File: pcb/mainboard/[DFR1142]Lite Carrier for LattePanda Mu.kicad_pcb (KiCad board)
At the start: 4 copper layers, 150 x 109 mm, 165 parts, among them J1 Conn_01x03_Pin, J10 Conn_01x03_Pin, J11 Conn_01x03_Pin, J12 Conn_01x04_Pin, J13 Conn_01x04_Pin, J14 Conn_01x03_Pin, J15 Bus_M.2_Socket_M, J16 Bus_M.2_Socket_E, J3 HDMI_A, J7 Conn_01x04_Pin, J78 Conn_01x02_Pin, J79 USB3_A, J8 Conn_01x03_Pin, J80 USB3_A, J81 USB_C_Receptacle_USB2.0_16P, J82 Conn_01x04_Pin, J83 Conn_01x02_Pin, J9 Conn_01x04_Pin, Q1 2N7002, Q2 2SK3018, Q3 2SK3018, Q4 2SK3018, Q8 2N7002, U1 TPAZ1023-04F, U10 ULC0524P, U11 ULC0524P, U12 ULC0524P, U15 SY8253ADC, U16 SY8253ADC, U2 TPAZ1023-04F, U3 ULC0524P, U4 ULC0524P, U5 ULC0524P, U78 ULC0524P, U9 ULC0524P

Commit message: a lot has been routed
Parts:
- moved C55 163.5 mm to (97.8, 137.0), turned to 90 degrees
- moved C56 161.3 mm to (96.8, 137.0), turned to 90 degrees
- moved J79 70.7 mm to (139.5, 155.3)
- moved J16 1.10 mm to (93.9, 118.0)
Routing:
- net /LattePanda Module/HSIO_3_TX-: track 0.00 -> 47.6 mm
- net /LattePanda Module/HSIO_3_TX+: track 0.00 -> 45.9 mm
- net /USB2.0&USB3.0/CON_USB4_SSRX_P: track 0.00 -> 40.2 mm, vias 0 -> 1
- net /USB2.0&USB3.0/CON_USB4_SSRX_N: track 0.00 -> 39.9 mm, vias 0 -> 1
- net /USB2.0&USB3.0/CON_USB3_SSRX_P: track 0.00 -> 35.4 mm, vias 0 -> 1
- net /USB2.0&USB3.0/CON_USB3_SSRX_N: track 0.00 -> 35.1 mm, vias 0 -> 1
- net /M.2 E&M Key/CON_PCIE_TX_0+: track 0.00 -> 11.6 mm, vias 0 -> 2
- net /M.2 E&M Key/CON_PCIE_TX_0-: track 0.00 -> 11.1 mm, vias 0 -> 2
- net /LattePanda Module/HSIO_3_RX-: track 43.1 -> 46.0 mm
- net /LattePanda Module/HSIO_3_RX+: track 42.5 -> 45.4 mm
- net /LattePanda Module/HSIO_2_RX+: track 30.0 -> 28.7 mm
- net /LattePanda Module/HSIO_2_RX-: track 29.7 -> 28.6 mm
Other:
- board size 150 x 109 mm -> 150.8 x 109 mm

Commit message: latest
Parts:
- moved U3 183.8 mm to (143.8, 148.1), turned to -90 degrees
- moved C26 167.1 mm to (142.5, 145.2), turned to -90 degrees
- moved C27 164.8 mm to (141.2, 145.2), turned to -90 degrees
- moved C28 142.4 mm to (101.0, 150.2), turned to -90 degrees
- moved C29 139.6 mm to (99.0, 150.2), turned to -90 degrees
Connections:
- U3 pad 1: /USB2.0&USB3.0/CON_USB3_SSRX_P -> /USB2.0&USB3.0/CON_USB3_SSRX_N
- U3 pad 10: /USB2.0&USB3.0/CON_USB3_SSRX_P -> /USB2.0&USB3.0/CON_USB3_SSRX_N
- U3 pad 2: /USB2.0&USB3.0/CON_USB3_SSRX_N -> /USB2.0&USB3.0/CON_USB3_SSRX_P
- U3 pad 4: /USB2.0&USB3.0/CON_USB3_SSTX_P -> /USB2.0&USB3.0/CON_USB3_SSTX_N
- U3 pad 5: /USB2.0&USB3.0/CON_USB3_SSTX_N -> /USB2.0&USB3.0/CON_USB3_SSTX_P
- U3 pad 6: /USB2.0&USB3.0/CON_USB3_SSTX_N -> /USB2.0&USB3.0/CON_USB3_SSTX_P
- U3 pad 7: /USB2.0&USB3.0/CON_USB3_SSTX_P -> /USB2.0&USB3.0/CON_USB3_SSTX_N
- U3 pad 9: /USB2.0&USB3.0/CON_USB3_SSRX_N -> /USB2.0&USB3.0/CON_USB3_SSRX_P
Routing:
- net /USB2.0&USB3.0/CON_USB3_D_N: track 0.00 -> 24.1 mm, vias 0 -> 1
- net /USB2.0&USB3.0/CON_USB3_D_P: track 0.00 -> 24.1 mm, vias 0 -> 1
- net /LattePanda Module/HSIO_0_TX-: track 0.00 -> 18.0 mm, vias 0 -> 2
- net /LattePanda Module/HSIO_0_TX+: track 0.00 -> 17.0 mm, vias 0 -> 2
- net /USB2.0&USB3.0/CON_USB3_SSTX_P: track 0.00 -> 10.6 mm
- net /USB2.0&USB3.0/CON_USB3_SSTX_N: track 0.00 -> 9.46 mm
- net /USB2.0&USB3.0/CON_USB3_SSRX_N: track 35.1 -> 36.0 mm, vias 1 -> 2
- net /USB2.0&USB3.0/CON_USB3_SSRX_P: track 35.4 -> 35.2 mm, vias 1 -> 2

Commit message: gtg sleep
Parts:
- moved U4 198.8 mm to (160.0, 155.6), turned to 90 degrees
- moved J81 197.2 mm to (156.3, 159.2)
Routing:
- net /USB2.0&USB3.0/CON_USB1_D_N: track 0.00 -> 39.0 mm
- net /USB2.0&USB3.0/CON_USB1_D_P: track 0.00 -> 38.1 mm

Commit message: gtg
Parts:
- moved H3 208.3 mm to (183.3, 162.5)
- moved J82 194.7 mm to (156.6, 141.5), turned to -90 degrees
- moved H4 128.6 mm to (89.2, 163.0)
- moved TP6 122.0 mm to (-31.4, 183.4)
- moved C71 122.0 mm to (-31.8, 193.6)
- moved C73 122.0 mm to (-31.8, 197.6)
- moved C77 122.0 mm to (-15.6, 183.3)
- moved C83 122.0 mm to (-11.6, 183.3)
- moved L2 122.0 mm to (-18.8, 193.0)
- moved R59 122.0 mm to (-8.65, 187.5)
- moved R60 122.0 mm to (-8.65, 189.5)
- moved U16 122.0 mm to (-27.1, 195.0)
- moved C75 122.0 mm to (-15.6, 178.3)
- moved C79 122.0 mm to (-31.8, 201.5)
- moved C81 122.0 mm to (-11.6, 178.3)
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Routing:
- net /USB2.0&USB3.0/CON_USB2_D_P: track 0.00 -> 11.1 mm
- net /USB2.0&USB3.0/CON_USB2_D_N: track 0.00 -> 10.2 mm
- net /HDMI/TMDS_D0-: track 20.8 -> 26.8 mm
- net /HDMI/TMDS_D0+: track 21.5 -> 26.8 mm
- net /HDMI/TMDS_D1-: track 22.1 -> 17.4 mm
- net /HDMI/TMDS_CK+: track 22.2 -> 26.9 mm
- net /HDMI/TMDS_CK-: track 22.0 -> 26.4 mm
- net /HDMI/TMDS_D1+: track 21.5 -> 17.5 mm
- net /USB2.0&USB3.0/CON_USB1_D_P: track 38.1 -> 40.5 mm
- net /HDMI/TMDS_D2+: track 22.0 -> 23.8 mm
- net /LattePanda Module/REFCLK0-: track 1.47 -> 0.00 mm
- net /LattePanda Module/REFCLK0+: track 1.47 -> 0.00 mm
- net /USB2.0&USB3.0/CON_USB1_D_N: track 39.0 -> 40.0 mm
- net /USB2.0&USB3.0/CON_USB3_D_P: track 24.1 -> 23.4 mm
- net /USB2.0&USB3.0/CON_USB3_D_N: track 24.1 -> 23.4 mm
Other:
- board size 150.8 x 109 mm -> 115.5 x 109 mm

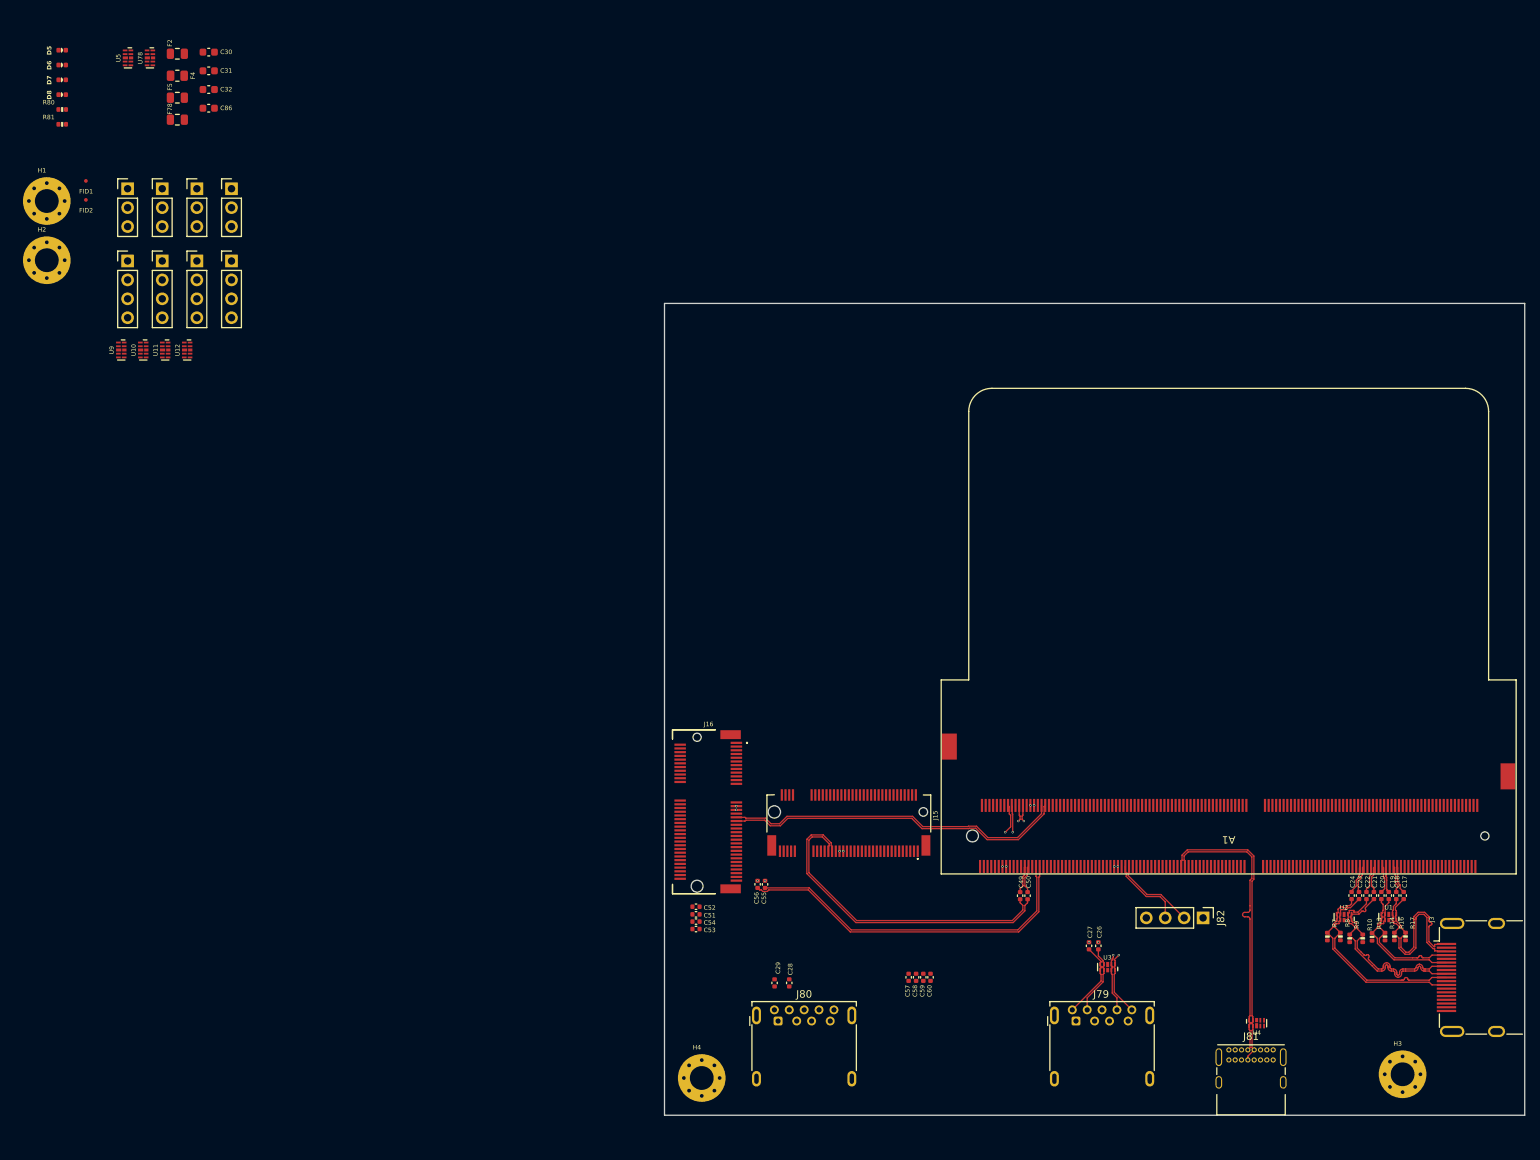
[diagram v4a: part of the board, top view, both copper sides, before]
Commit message: most length matching almost done
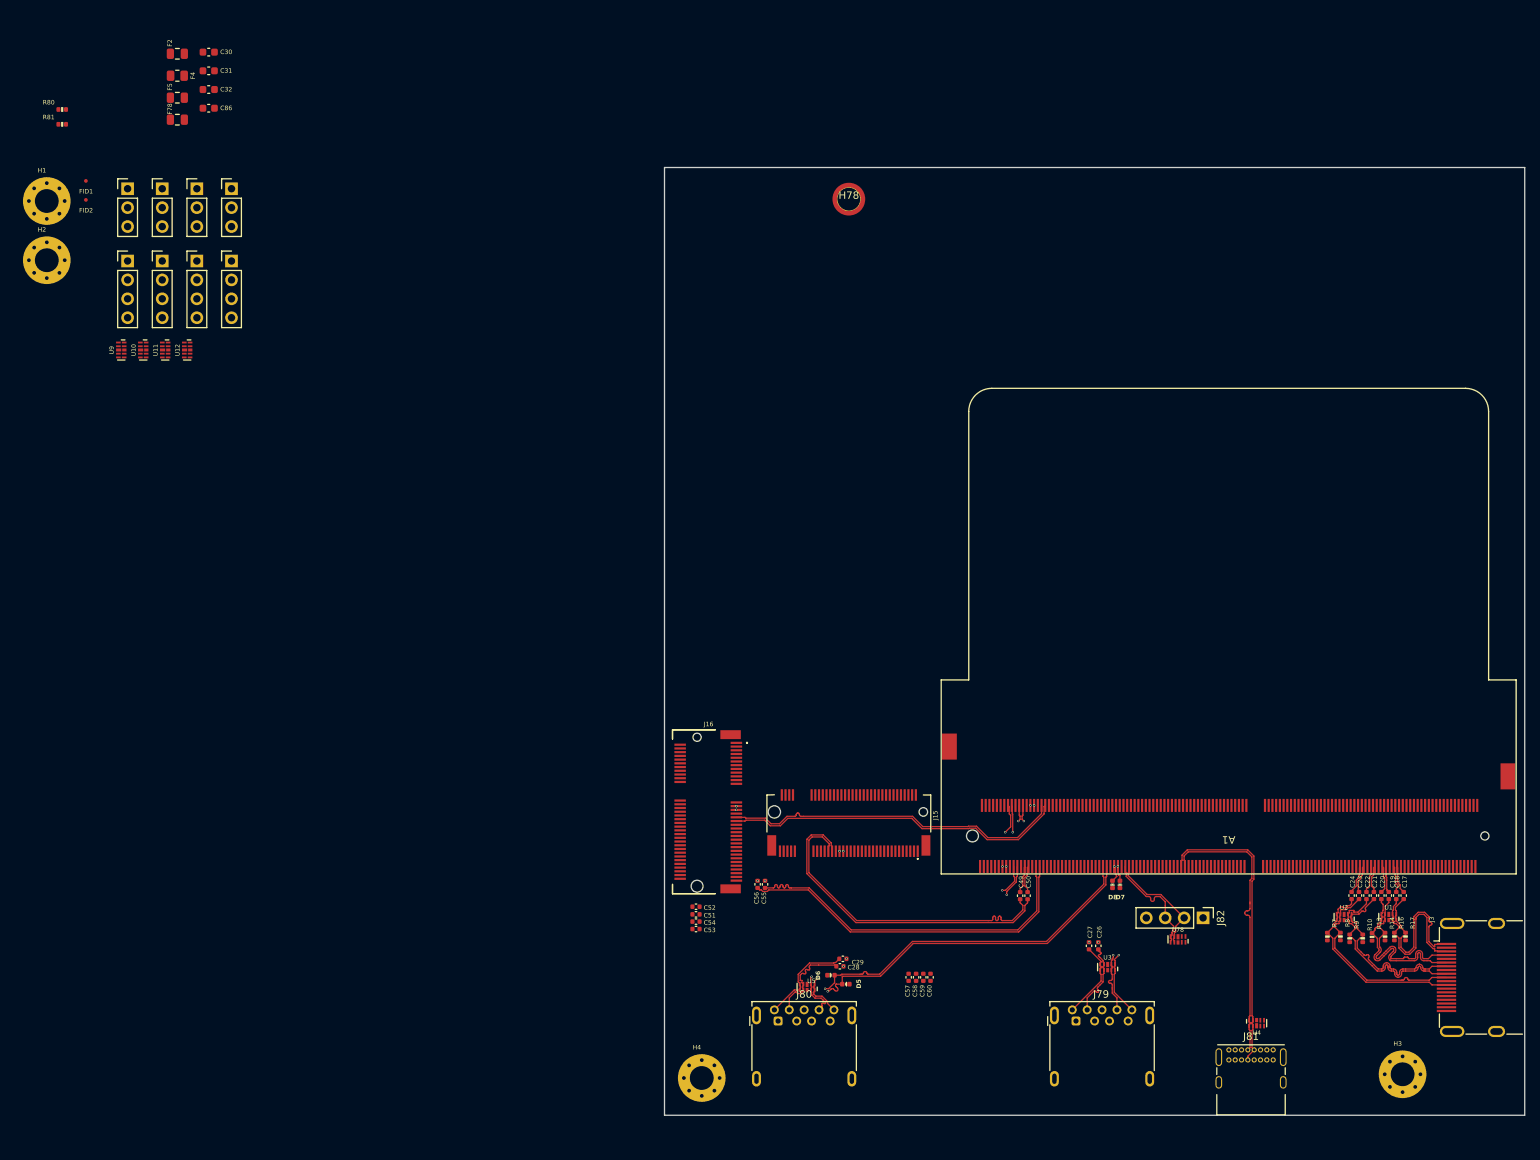
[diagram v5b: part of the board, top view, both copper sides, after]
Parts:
- added H78: MountingHole_Pad, A_HDJ_Library:MountingHole_3mm_M2_Pad_TopOnly, F.Cu at (109.0, 45.0)
- moved U78 181.8 mm to (153.2, 144.4), turned to -90 degrees
- moved D7 178.4 mm to (145.4, 137.0), turned to 90 degrees
- moved D8 176.4 mm to (144.4, 137.0), turned to 90 degrees
- moved D5 163.7 mm to (108.6, 150.4), turned to 180 degrees
- moved D6 160.0 mm to (106.6, 149.2)
- moved U5 154.5 mm to (103.4, 150.8), turned to -90 degrees
- moved C29 9.72 mm to (108.2, 147.0), turned to 180 degrees
- moved C28 7.16 mm to (107.8, 148.0), turned to 180 degrees
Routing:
- net /USB2.0&USB3.0/CON_USB4_D_N: track 0.00 -> 53.8 mm, vias 0 -> 1
- net /USB2.0&USB3.0/CON_USB4_D_P: track 0.00 -> 53.8 mm, vias 0 -> 1
- net /LattePanda Module/HSIO_1_TX-: track 0.00 -> 41.2 mm, vias 0 -> 2
- net /LattePanda Module/HSIO_1_TX+: track 0.00 -> 41.1 mm, vias 0 -> 2
- net /USB2.0&USB3.0/CON_USB4_SSTX_P: track 0.00 -> 13.2 mm
- net /USB2.0&USB3.0/CON_USB4_SSTX_N: track 0.00 -> 13.1 mm
- net /HDMI/TMDS_D1-: track 17.4 -> 24.1 mm
- net /USB2.0&USB3.0/CON_USB4_SSRX_P: track 40.2 -> 46.8 mm, vias 1 -> 2
- net /HDMI/TMDS_D1+: track 17.5 -> 24.0 mm
- net /USB2.0&USB3.0/CON_USB4_SSRX_N: track 39.9 -> 46.0 mm, vias 1 -> 2
- net /USB2.0&USB3.0/CON_USB2_D_N: track 10.2 -> 15.1 mm
- net /USB2.0&USB3.0/CON_USB2_D_P: track 11.1 -> 15.1 mm
- net /USB2.0&USB3.0/CON_USB3_D_N: track 23.4 -> 25.8 mm
- net /USB2.0&USB3.0/CON_USB3_D_P: track 23.4 -> 25.5 mm
- net /M.2 E&M Key/CON_PCIE_TX_1+: track 42.3 -> 44.0 mm
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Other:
- board size 115.5 x 109 mm -> 115.5 x 127.2 mm
